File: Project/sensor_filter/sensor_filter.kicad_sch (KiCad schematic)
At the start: 20 parts, among them IC1 MCP601-E_SN, IC2 MCP601-E_SN, IC3 MCP601-E_SN, IC4 MCP601-E_SN, J1 Conn_01x08_Socket, J2 Screw_Terminal_01x02, J3 Conn_01x04_Socket, J4 Conn_01x04_Socket

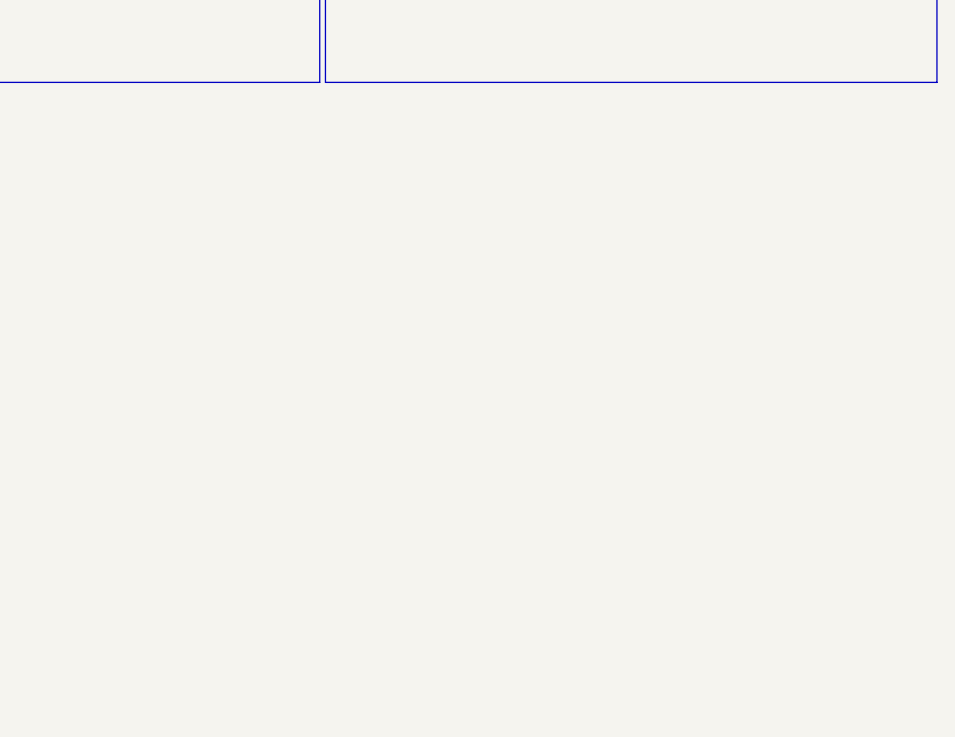
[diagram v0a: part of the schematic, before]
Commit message: Izhikevich for Arduino
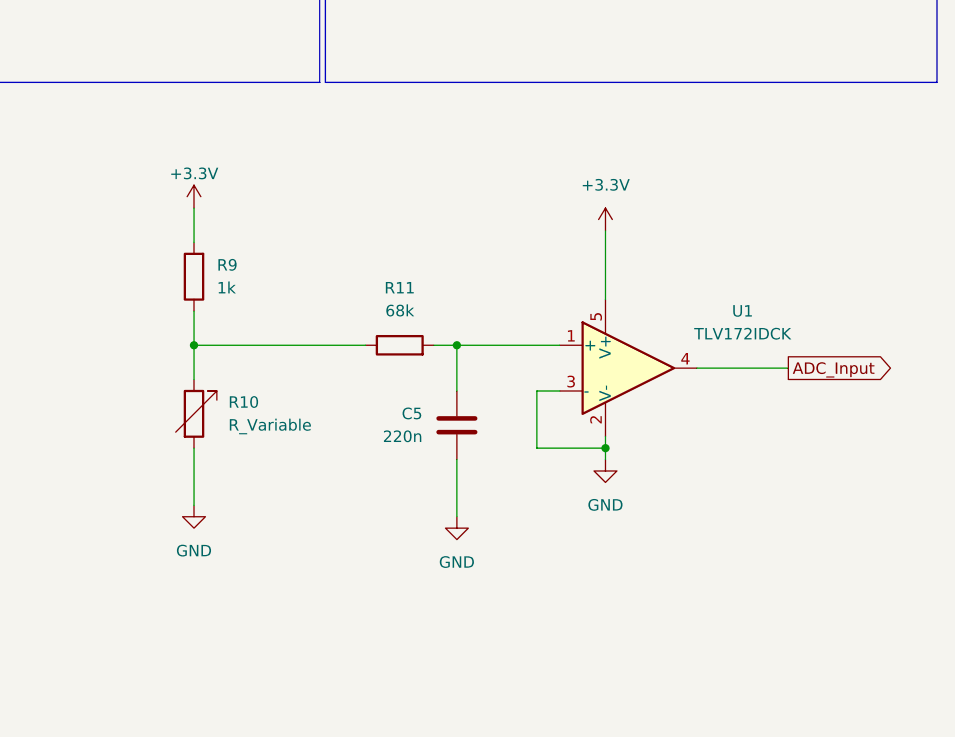
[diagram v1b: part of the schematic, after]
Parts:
- added C5: 220n, Capacitor_THT:CP_Radial_Tantal_D4.5mm_P2.50mm, symbol Device:C
- added R10: R_Variable, symbol Device:R_Variable
- added R11: 68k, Resistor_THT:R_Axial_DIN0207_L6.3mm_D2.5mm_P7.62mm_Horizontal, symbol Device:R
- added R9: 1k, Resistor_THT:R_Axial_DIN0207_L6.3mm_D2.5mm_P7.62mm_Horizontal, symbol Device:R
- added U1: TLV172IDCK, Package_TO_SOT_SMD:SOT-353_SC-70-5, symbol Amplifier_Operational:TLV172IDCK
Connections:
- net +3.3V: now also R9.2, U1.5 (V+)
- net GND: now also C5.2, R10.2, U1.2 (V-), U1.3 (-)
- new net: R10.1, R11.1, R9.1
- new net: C5.1, R11.2, U1.1 (+)
- new net ADC_Input: U1.4

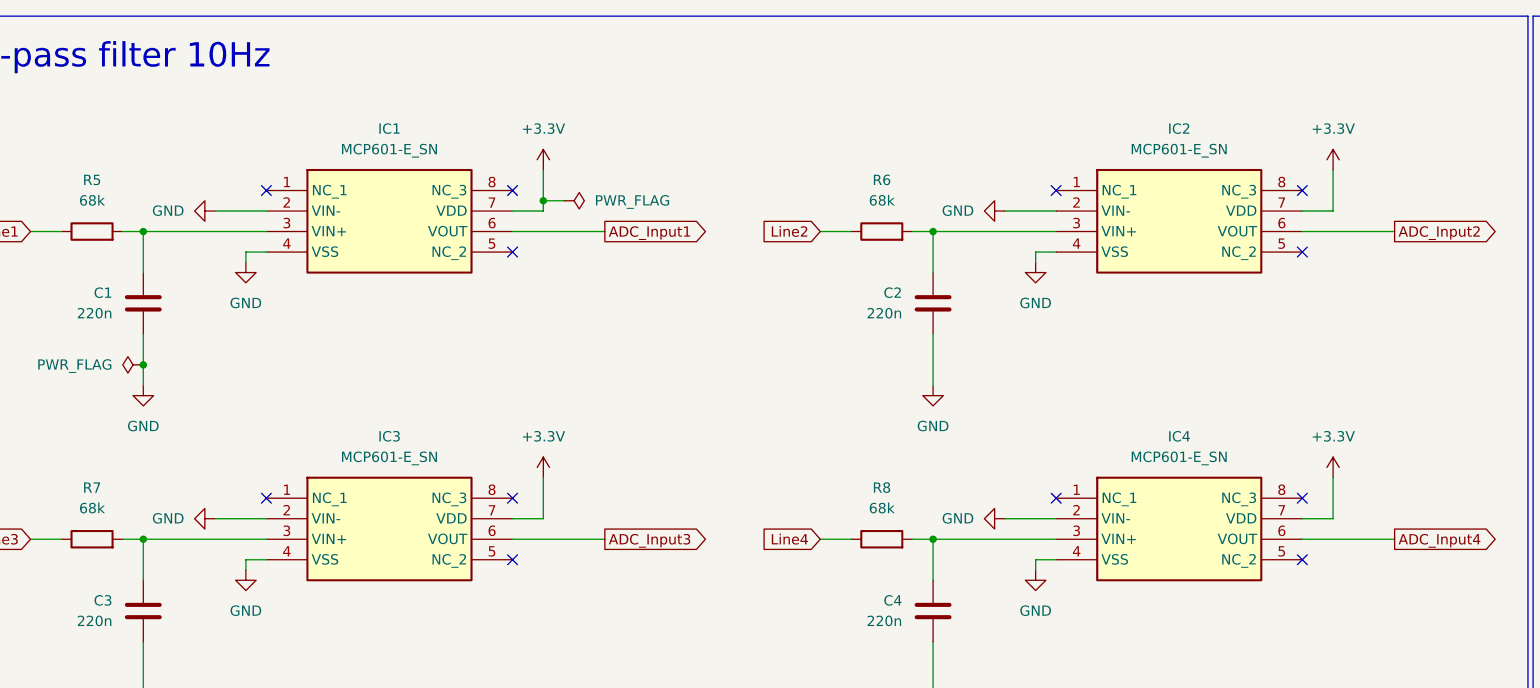
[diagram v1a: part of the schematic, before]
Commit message: Inclusao da placa de aquisicao
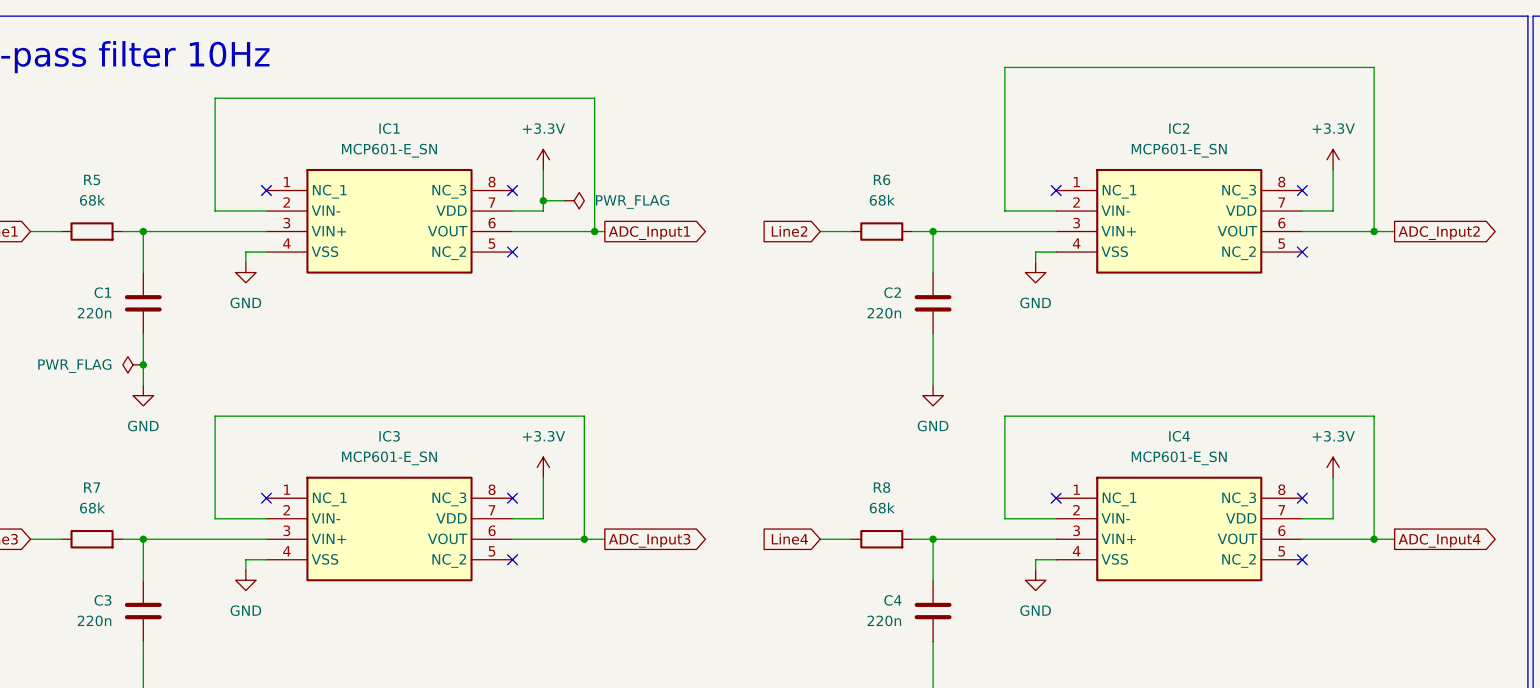
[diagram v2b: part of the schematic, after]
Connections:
- net ADC_Input1: now also IC1.2 (VIN-)
- net ADC_Input2: now also IC2.2 (VIN-)
- net ADC_Input3: now also IC3.2 (VIN-)
- net ADC_Input4: now also IC4.2 (VIN-)
- net GND: no longer IC1.2 (VIN-), IC2.2 (VIN-), IC3.2 (VIN-), IC4.2 (VIN-)
